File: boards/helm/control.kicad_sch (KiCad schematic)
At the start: 38 parts, among them J11 AS5600, J12 PICO UTIL, J13 THRUST DRV, J22 SERVO MOTOR, U1 Pico 2, U7 BTN8982TA, U8 BTN8982TA

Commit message: feat(gen_sheet): drawn wires + power rails (WIRES/RAILS spec lists) with per-cluster label dedup; wire up power chain, VIN rail, N2K links, sense rails, SR/LED chains
Co-Authored-By: Claude Fable 5 <noreply@anthropic.com>
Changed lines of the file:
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@@
     (instances (project "vanchor-helm" (path "/a0000000-0000-4000-8000-000000000001/c0000000-0000-4000-8000-000000000004" (reference "J11") (unit 1))))
   )
+  (wire (pts (xy 49.53 256.54) (xy 40.64 256.54))
+    (stroke (width 0) (type default)))
+  (wire (pts (xy 40.64 256.54) (xy 40.64 281.94))
+    (stroke (width 0) (type default)))
+  (wire (pts (xy 124.46 256.54) (xy 91.44 256.54))
+    (stroke (width 0) (type default)))
+  (wire (pts (xy 91.44 256.54) (xy 91.44 281.94))
+    (stroke (width 0) (type default)))
+  (wire (pts (xy 378.46 181.61) (xy 388.62 181.61))
+    (stroke (width 0) (type default)))
+  (wire (pts (xy 388.62 181.61) (xy 388.62 212.09))
+    (stroke (width 0) (type default)))
+  (wire (pts (xy 199.39 212.09) (xy 199.39 204.47))
+    (stroke (width 0) (type default)))
+  (wire (pts (xy 241.3 212.09) (xy 241.3 204.47))
+    (stroke (width 0) (type default)))
+  (wire (pts (xy 290.83 212.09) (xy 290.83 204.47))
+    (stroke (width 0) (type default)))
+  (wire (pts (xy 199.39 204.47) (xy 290.83 204.47))
+    (stroke (width 0) (type default)))
+  (wire (pts (xy 146.05 196.85) (xy 146.05 190.5))
+    (stroke (width 0) (type default)))
+  (wire (pts (xy 205.74 196.85) (xy 205.74 190.5))
+    (stroke (width 0) (type default)))
+  (wire (pts (xy 264.16 196.85) (xy 264.16 190.5))
+    (stroke (width 0) (type default)))
+  (wire (pts (xy 146.05 190.5) (xy 264.16 190.5))
+    (stroke (width 0) (type default)))
+  (junction (at 199.39 204.47) (diameter 0) (color 0 0 0 0)
+)
+  (junction (at 241.3 204.47) (diameter 0) (color 0 0 0 0)
+)
+  (junction (at 290.83 204.47) (diameter 0) (color 0 0 0 0)
+)
+  (junction (at 146.05 190.5) (diameter 0) (color 0 0 0 0)
+)
+  (junction (at 205.74 190.5) (diameter 0) (color 0 0 0 0)
+)
+  (junction (at 264.16 190.5) (diameter 0) (color 0 0 0 0)
+)
   (global_label "PICO_GP0" (shape passive) (at 72.39 104.14 180.0) (fields_autoplaced yes)
     (effects (font (size 1.27 1.27)) (justify right))
@@
       (effects (font (size 1.27 1.27)) (hide yes)))
   )
-  (global_label "VBAT_SENSE" (shape passive) (at 241.3 212.09 180.0) (fields_autoplaced yes)
-    (effects (font (size 1.27 1.27)) (justify right))
-    (property "Intersheetrefs" "${INTERSHEET_REFS}" (at 241.3 212.09 0)
-      (effects (font (size 1.27 1.27)) (hide yes)))
-  )
   (global_label "GND" (shape passive) (at 248.92 212.09 0.0) (fields_autoplaced yes)
     (effects (font (size 1.27 1.27)) (justify left))
@@
       (effects (font (size 1.27 1.27)) (hide yes)))
   )
-  (global_label "VBAT_SENSE" (shape passive) (at 290.83 212.09 180.0) (fields_autoplaced yes)
-    (effects (font (size 1.27 1.27)) (justify right))
-    (property "Intersheetrefs" "${INTERSHEET_REFS}" (at 290.83 212.09 0)
-      (effects (font (size 1.27 1.27)) (hide yes)))
-  )
   (global_label "GND" (shape passive) (at 298.45 212.09 0.0) (fields_autoplaced yes)
     (effects (font (size 1.27 1.27)) (justify left))
@@
     (effects (font (size 1.27 1.27)) (justify left))
   )
-  (label "LED5_A" (at 388.62 212.09 0.0) (fields_autoplaced yes)
-    (effects (font (size 1.27 1.27)) (justify left))
-  )
   (global_label "GND" (shape passive) (at 381 212.09 180.0) (fields_autoplaced yes)
     (effects (font (size 1.27 1.27)) (justify right))
@@
       (effects (font (size 1.27 1.27)) (hide yes)))
   )
-  (global_label "HALL_ZERO" (shape passive) (at 205.74 196.85 180.0) (fields_autoplaced yes)
-    (effects (font (size 1.27 1.27)) (justify right))
-    (property "Intersheetrefs" "${INTERSHEET_REFS}" (at 205.74 196.85 0)
-      (effects (font (size 1.27 1.27)) (hide yes)))
-  )
   (global_label "PICO_GP0" (shape passive) (at 213.36 196.85 0.0) (fields_autoplaced yes)
     (effects (font (size 1.27 1.27)) (justify left))
@@
       (effects (font (size 1.27 1.27)) (hide yes)))
   )
-  (global_label "HALL_ZERO" (shape passive) (at 264.16 196.85 180.0) (fields_autoplaced yes)
-    (effects (font (size 1.27 1.27)) (justify right))
-    (property "Intersheetrefs" "${INTERSHEET_REFS}" (at 264.16 196.85 0)
-      (effects (font (size 1.27 1.27)) (hide yes)))
-  )
   (global_label "GND" (shape passive) (at 271.78 196.85 0.0) (fields_autoplaced yes)
     (effects (font (size 1.27 1.27)) (justify left))
@@
       (effects (font (size 1.27 1.27)) (hide yes)))
   )
-  (label "SR_A" (at 40.64 281.94 180.0) (fields_autoplaced yes)
-    (effects (font (size 1.27 1.27)) (justify right))
-  )
   (global_label "GND" (shape passive) (at 48.26 281.94 0.0) (fields_autoplaced yes)
     (effects (font (size 1.27 1.27)) (justify left))
@@
       (effects (font (size 1.27 1.27)) (hide yes)))
   )
-  (label "SR_B" (at 91.44 281.94 180.0) (fields_autoplaced yes)
-    (effects (font (size 1.27 1.27)) (justify right))
-  )
   (global_label "GND" (shape passive) (at 99.06 281.94 0.0) (fields_autoplaced yes)

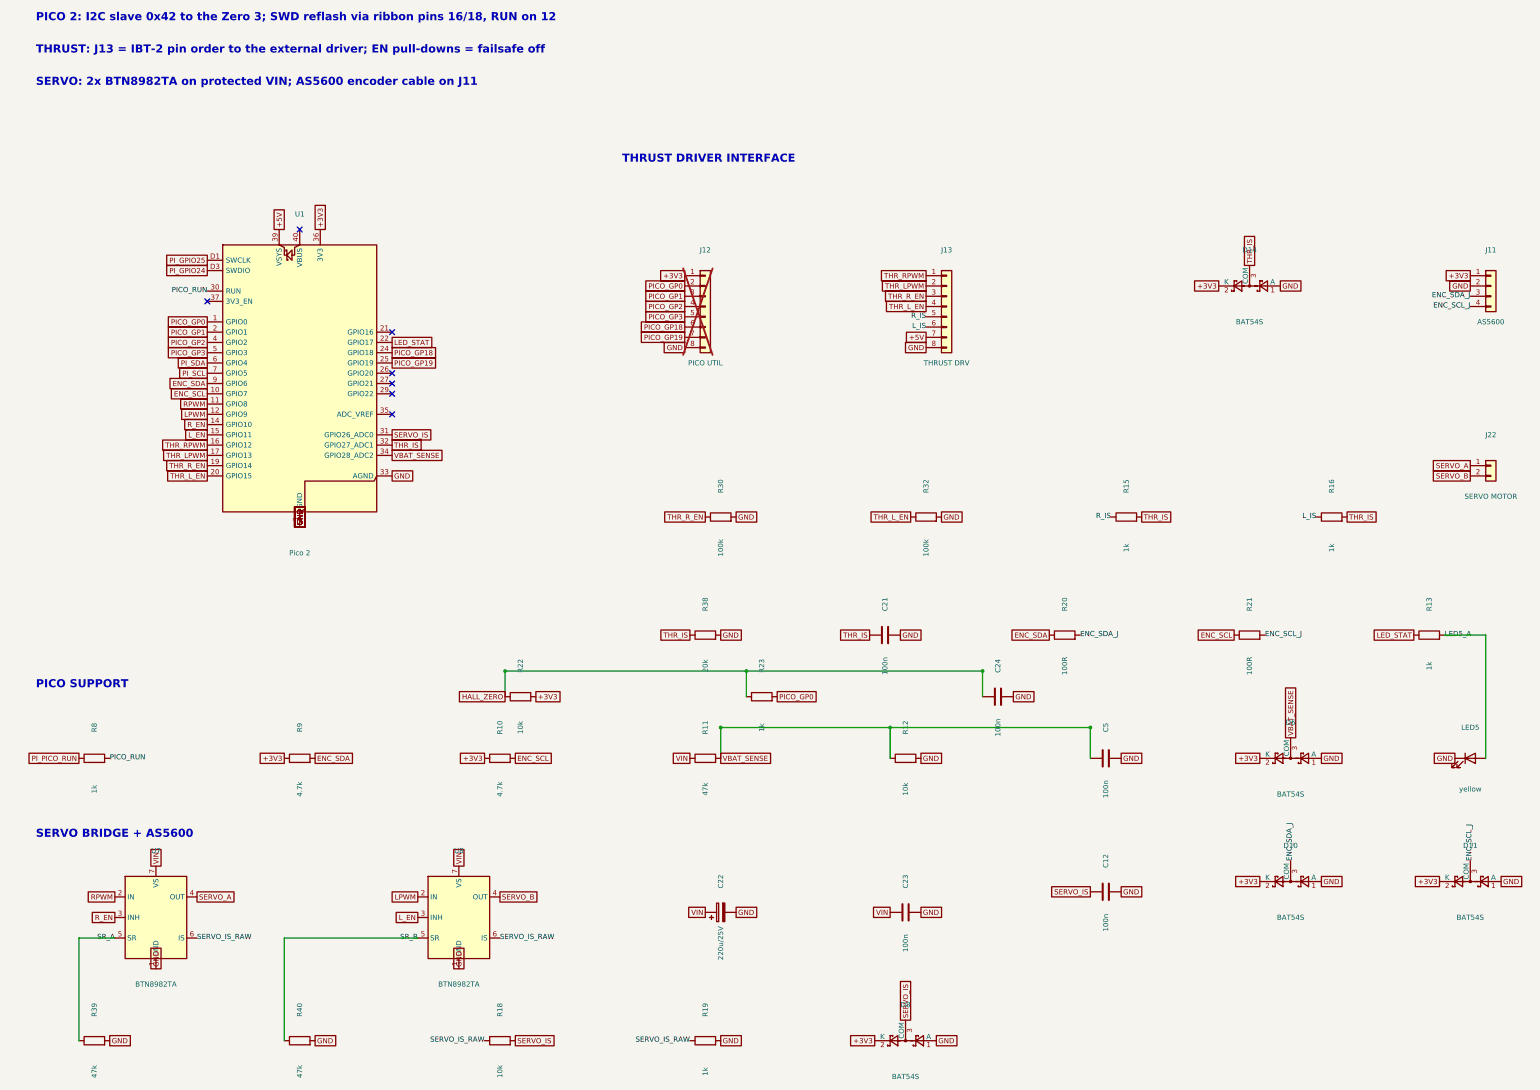
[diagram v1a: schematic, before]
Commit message: feat(schematics): wire the Pico to its peripherals on both boards
Helm control page: GP0-3 bus to J12, 4-wire thrust bus to J13 (nested
staircase under the pico), RPWM/LPWM to the servo bridge inputs,
LED_STAT to R13, VBAT_SENSE over the arrivals down to the divider rail.
Driver page: DNP-pico CAN pair to J6, IS-to-ADC series R12/R13.
gen_sheet.py: turtle-style waypoint routing for WIRES (("x"/"y", v)
segments + auto-L tail); layout shuffle so J12/J13 flank the pico.

Co-Authored-By: Claude Fable 5 <noreply@anthropic.com>
Claude-Session: https://claude.ai/code/session_011PT4Xv5KGhDdDc8nqJyMxJ
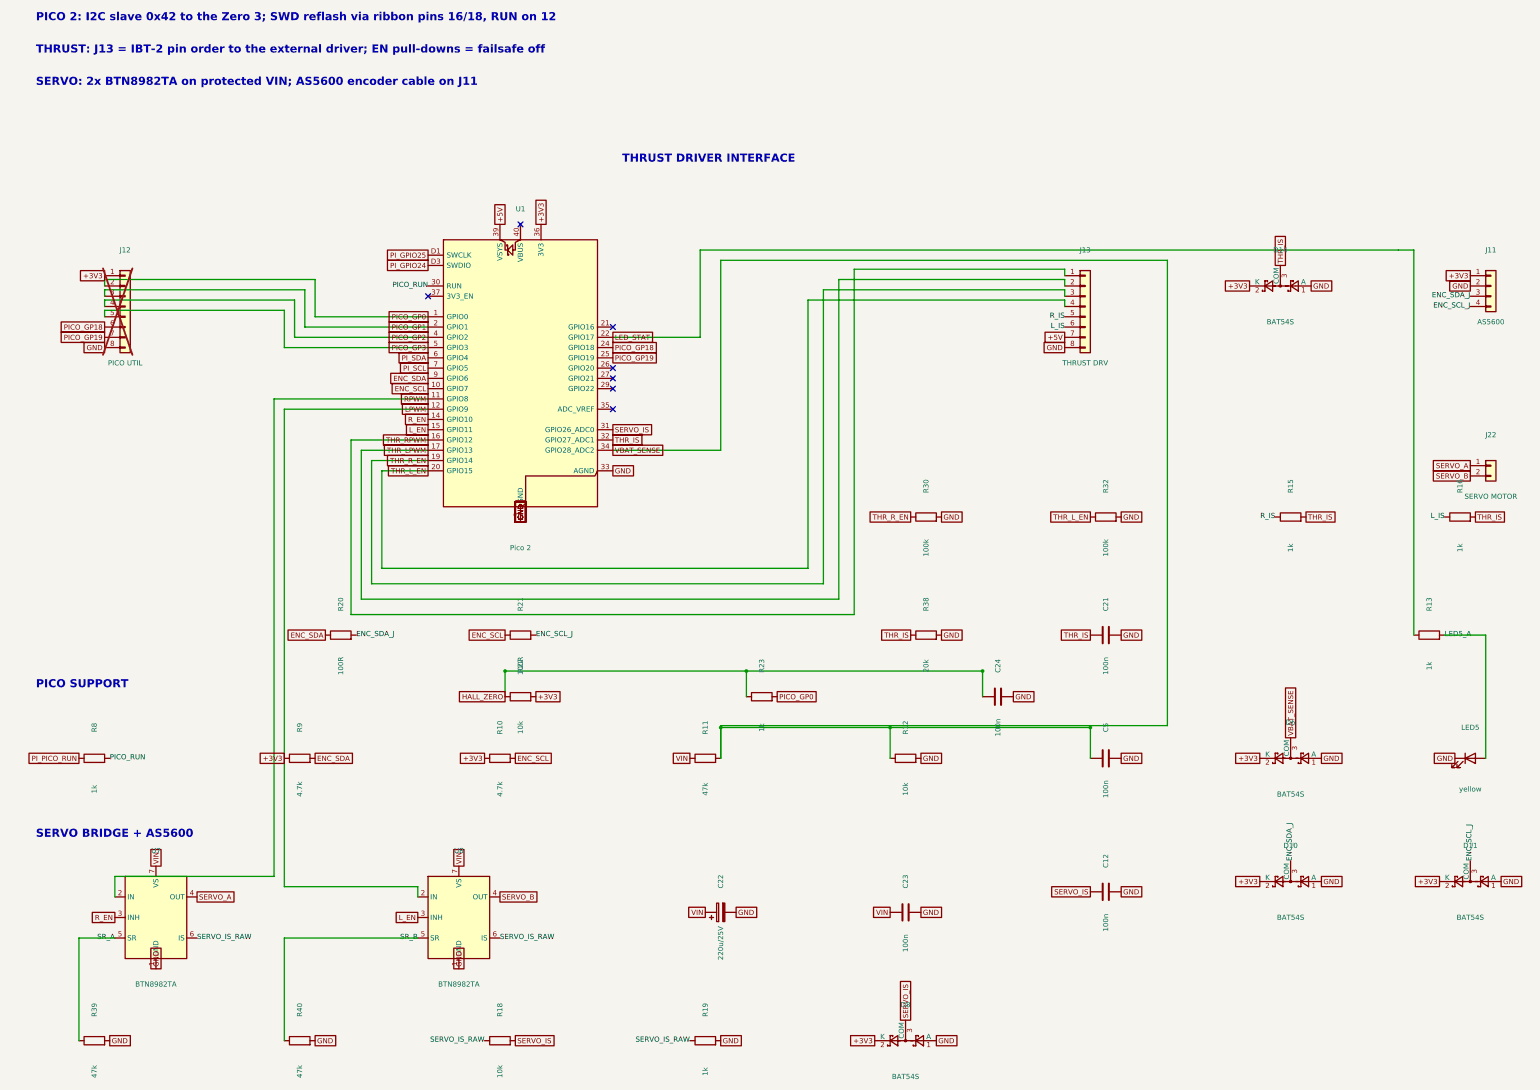
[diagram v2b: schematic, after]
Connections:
- net LPWM is gone; now on net +3V3: U1.12 (GPIO9), U8.2 (IN)
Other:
- moved on the sheet: C21, D14, J12, J13, R15, R16, R20, R21, R30, R32, R38, U1
